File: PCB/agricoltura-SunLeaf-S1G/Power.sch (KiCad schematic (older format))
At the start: 0 parts

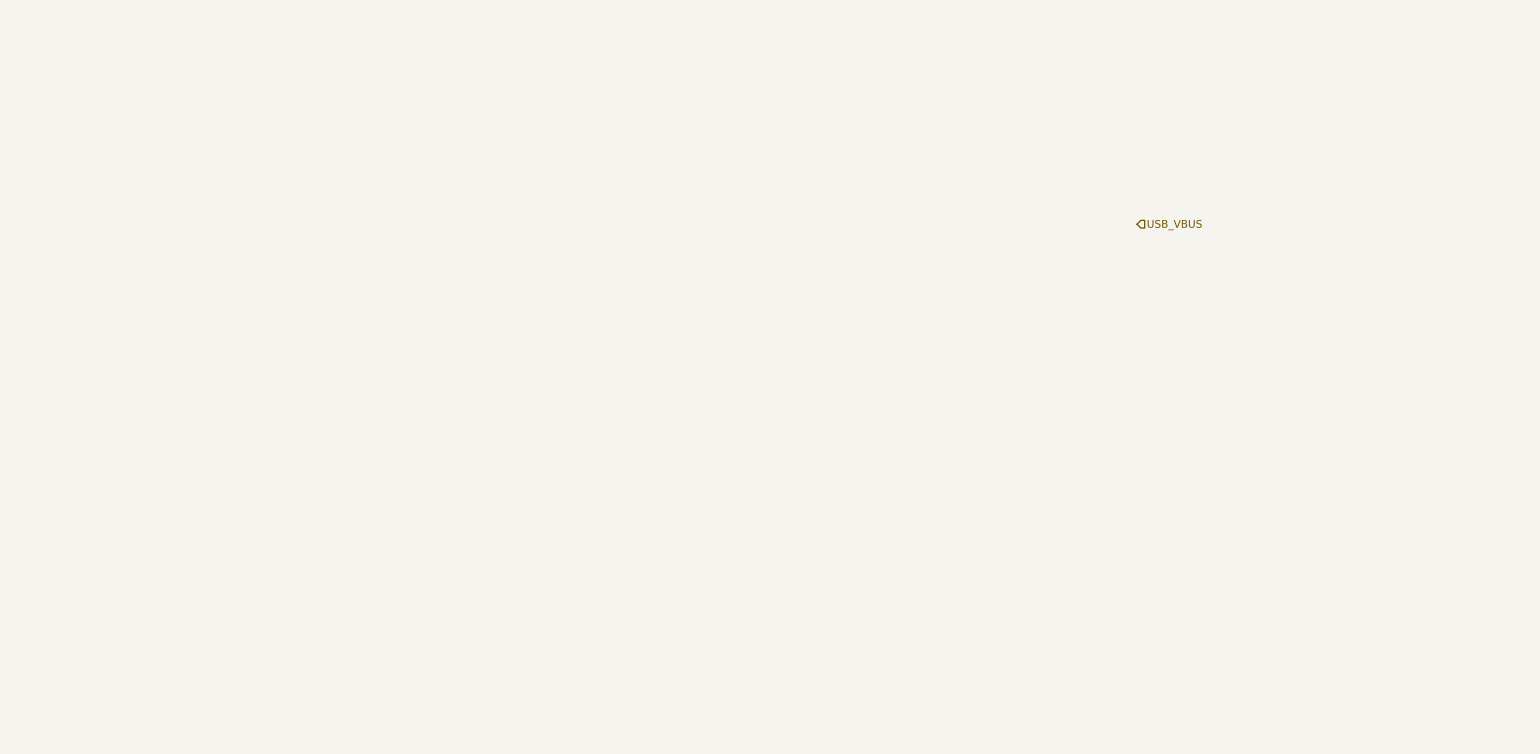
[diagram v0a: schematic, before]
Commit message: Power Supply and Datasheets
Added datasheets for parts in use, designed power supply circuit
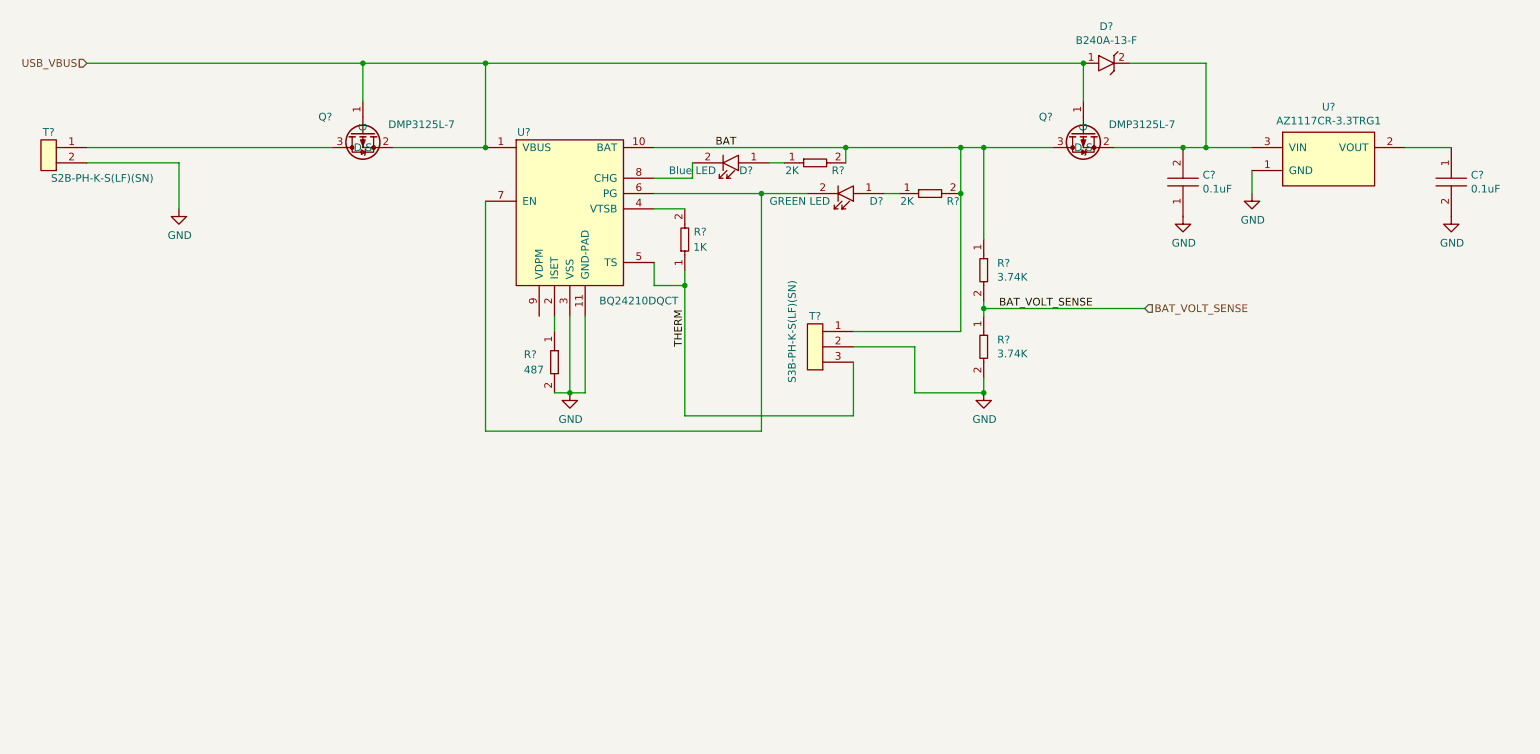
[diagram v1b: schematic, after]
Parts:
- added C?: C0402C104K9PACTU, AVR-KiCAD-Lib-Resistors:R0402, symbol AVR-KiCAD-Lib-Capacitors:C0402C104K9PACTU
- added C?: C0805C104M5RACTU, AVR-KiCAD-Lib-Capacitors:C0805, symbol AVR-KiCAD-Lib-Capacitors:C0805C104M5RACTU
- added D?: LTST-C194TBKT, AVR-KiCAD-Lib-Diodes:LED0603, symbol AVR-KiCAD-Lib-Diodes:LTST-C194TBKT
- added D?: LTST-C194KGKT, AVR-KiCAD-Lib-Diodes:LED0603, symbol AVR-KiCAD-Lib-Diodes:LTST-C194KGKT
- added D?: B240A-13-F, AVR-KiCAD-Lib-Diodes:B240A-13-F, symbol AVR-KiCAD-Lib-Diodes:B240A-13-F
- added Q? (x2): DMP3125L-7, growbox-KiCAD-Transistors:SOT-23, symbol AVR-KiCAD-Lib-Transistors:DMP3125L-7
- added R? (x2): RC0402FR-072KL, AVR-KiCAD-Lib-Resistors:R0402, symbol AVR-KiCAD-Lib-Resistors:RC0402FR-072KL
- added R?: RC0402FR-071KL, AVR-KiCAD-Lib-Resistors:R0402, symbol AVR-KiCAD-Lib-Resistors:RC0402FR-071KL
- added R? (x2): ERA-3AEB3741V, AVR-KiCAD-Lib-Resistors:R0603, symbol AVR-KiCAD-Lib-Resistors:ERA-3AEB3741V
- added R?: RC0402FR-07487RL, AVR-KiCAD-Lib-Resistors:R0402, symbol AVR-KiCAD-Lib-Resistors:RC0402FR-07487RL
- added T?: S2B-PH-K-S(LF)(SN), AVR-KiCAD-Lib-Connectors:S2B-PH-K-S(LF)(SN), symbol AVR-KiCAD-Lib-Connectors:S2B-PH-K-S(LF)(SN)
- added T?: S3B-PH-K-S(LF)(SN), AVR-KiCAD-Lib-Connectors:S3B-PH-K-S(LF)(SN), symbol AVR-KiCAD-Lib-Connectors:S3B-PH-K-S(LF)(SN)
- added U?: BQ24210DQCT, growbox-KiCAD-ICs:BQ24210, symbol AVR-KiCAD-Lib-ICs:BQ24210DQCT
- added U?: AZ1117CR-3.3TRG1, AVR-KiCAD-Lib-ICs:SOT_89, symbol AVR-KiCAD-Lib-ICs:AZ1117CR-3.3TRG1
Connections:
- net USB_VBUS: now also D?.1, Q?.1 (G), Q?.1 (G), Q?.2 (S), U?.1 (VBUS)
- new net: Q?.3 (D), T?.1
- new net: R?.1, U?.2 (ISET)
- new net: R?.2, U?.4 (VTSB)
- new net: D?.2, U?.6 (PG), U?.7 (EN)
- new net: D?.2, U?.8 (CHG)
- new net: D?.1, R?.1 (x2)
- new net: C?.1, U?.2 (VOUT)
- new net: C?.2, D?.2, Q?.2 (S), U?.3 (VIN)
- new net BAT: Q?.3 (D), R?.1, R?.2, R?.2, T?.1, U?.10 (BAT)
- new net BAT_VOLT_SENSE: R?.1, R?.2
- new net GND: C?.1, C?.2, R?.2, R?.2, T?.2, T?.2, U?.1 (GND), U?.11 (GND-PAD), U?.3 (VSS)
- new net THERM: R?.1, T?.3, U?.5 (TS)

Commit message: Schematic Complete
Schematic completed and PCB started
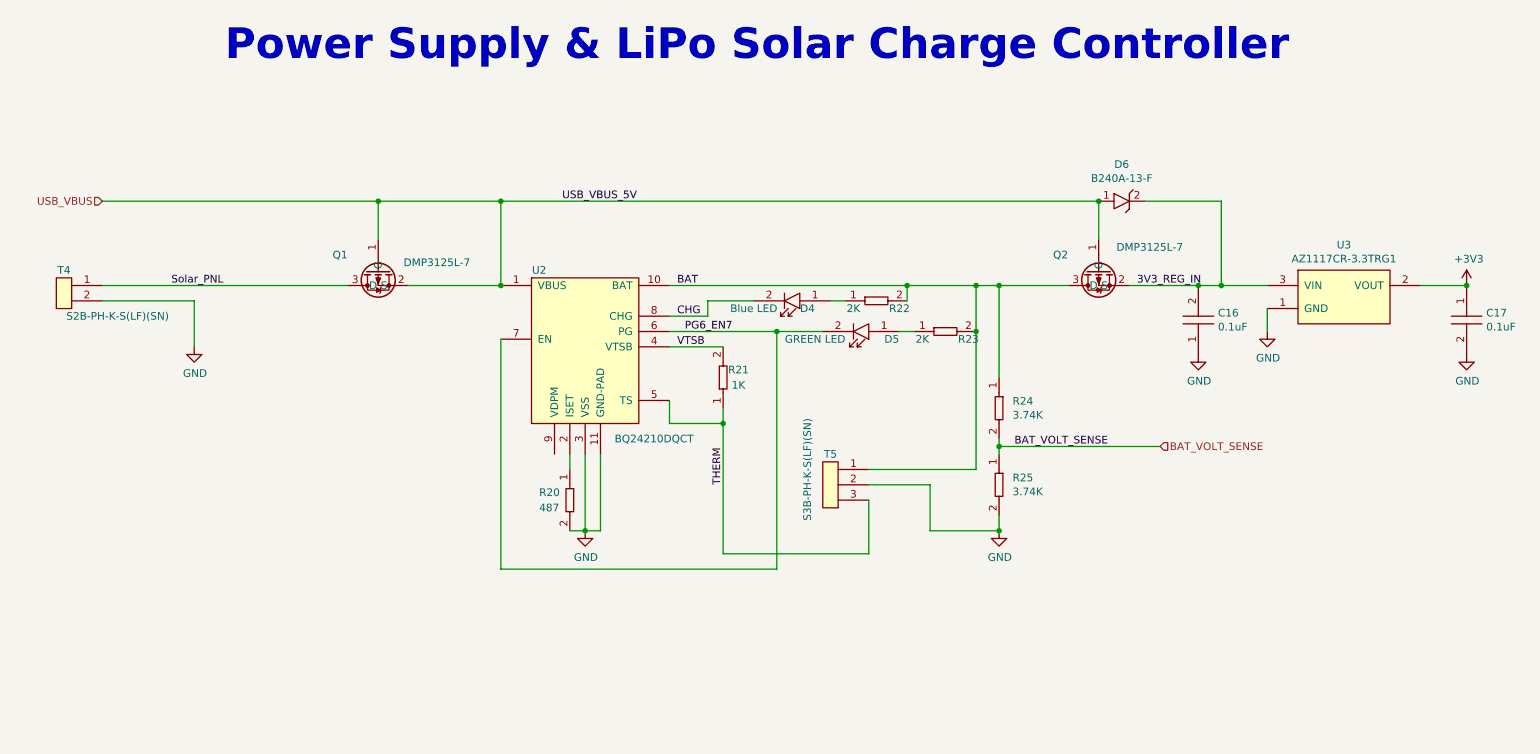
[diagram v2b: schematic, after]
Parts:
- gave numbers to parts that had none: 17
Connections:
- net Solar_PNL: now reaches Q1.3 (D), T4.1
- net VTSB: now reaches R21.2, U2.4 (VTSB)
- net PG6_EN7: now reaches D5.2, U2.6 (PG), U2.7 (EN)
- net CHG: now reaches D4.2, U2.8 (CHG)
- net +3V3: now reaches C17.1, U3.2 (VOUT)
- net 3V3_REG_IN: now reaches C16.2, D6.2, Q2.2 (S), U3.3 (VIN)
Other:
- note added: "Power Supply & LiPo Solar Charge Controller"
- moved on the sheet: C16, C17, D4, D5, D6, Q1, Q2, R20, R21, R22, R23, R24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

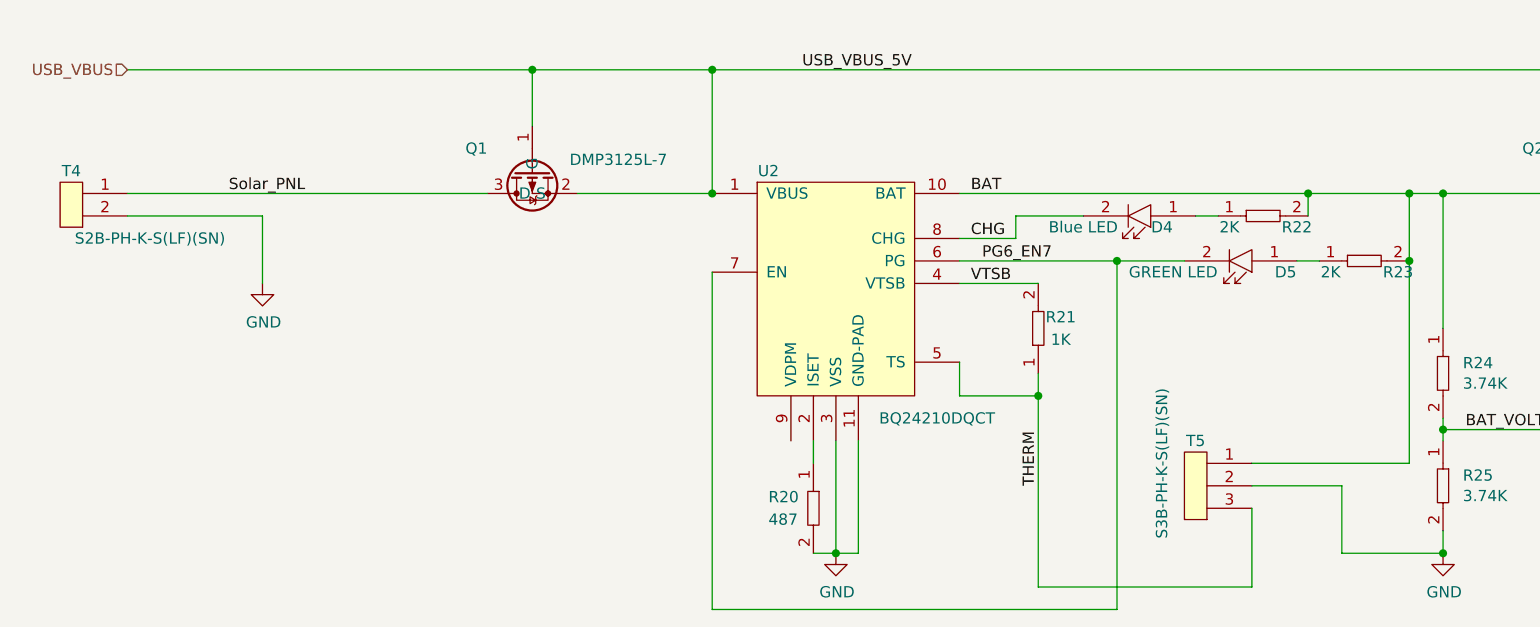
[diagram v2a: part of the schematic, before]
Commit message: PCB Progress
added TVS diodes fo QWIIC connector serial signals. Did more routing overall.
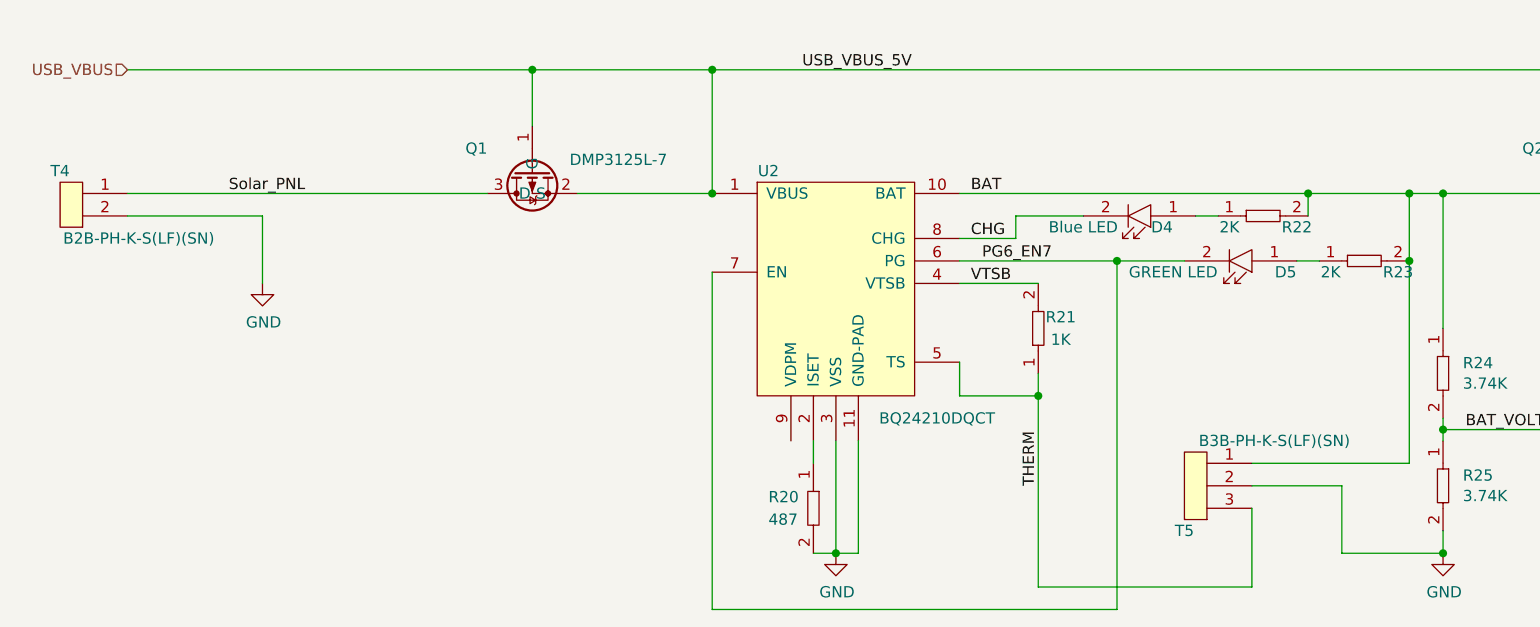
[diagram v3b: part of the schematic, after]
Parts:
- removed T4: S2B-PH-K-S(LF)(SN), AVR-KiCAD-Lib-Connectors:S2B-PH-K-S(LF)(SN), symbol AVR-KiCAD-Lib-Connectors:S2B-PH-K-S(LF)(SN)
- removed T5: S3B-PH-K-S(LF)(SN), AVR-KiCAD-Lib-Connectors:S3B-PH-K-S(LF)(SN), symbol AVR-KiCAD-Lib-Connectors:S3B-PH-K-S(LF)(SN)
- added T4: B2B-PH-K-S(LF)(SN), AVR-KiCAD-Lib-Connectors:B2B-PH-K-S(LF)(SN), symbol AVR-KiCAD-Lib-Connectors:B2B-PH-K-S(LF)(SN)
- added T5: B3B-PH-K-S(LF)(SN), AVR-KiCAD-Lib-Connectors:B3B-PH-K-S(LF)(SN), symbol AVR-KiCAD-Lib-Connectors:B3B-PH-K-S(LF)(SN)
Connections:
- net BAT: now also T5.1
- net GND: now also T4.2, T5.2
- net Solar_PNL: now also T4.1
- net THERM: now also T5.3
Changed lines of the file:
@@
-$EndComp
-$Comp
-L AVR-KiCAD-Lib-Connectors:S3B-PH-K-S(LF)(SN) T5
-U 1 1 5F07EF2F
-P 6400 4900
-F 0 "T5" H 6450 4950 50  0000 C CNN
-F 1 "S3B-PH-K-S(LF)(SN)" V 6300 4850 50  0000 C CNN
-F 2 "AVR-KiCAD-Lib-Connectors:S3B-PH-K-S(LF)(SN)" H 5100 5950 50  0001 C CNN
-F 3 "http://www.jst-mfg.com/product/pdf/eng/ePH.pdf" H 6300 5000 50  0001 C CNN
-F 4 "0.18000" H 6500 5150 50  0001 C CNN "Cost QTY: 1"
-F 5 "0.08119" H 6600 5250 50  0001 C CNN "Cost QTY: 1000"
-F 6 "*" H 6700 5350 50  0001 C CNN "Cost QTY: 2500"
-F 7 "0.07217" H 6800 5450 50  0001 C CNN "Cost QTY: 5000"
-F 8 "0.06541" H 6900 5550 50  0001 C CNN "Cost QTY: 10000"
-F 9 "JST Sales America Inc." H 7000 5650 50  0001 C CNN "MFR"
-F 10 "S3B-PH-K-S(LF)(SN)" H 7100 5750 50  0001 C CNN "MFR#"
-F 11 "Digikey" H 7200 5850 50  0001 C CNN "Vendor"
-F 12 "455-1720-ND" H 7300 5950 50  0001 C CNN "Vendor #"
-F 13 "AVR" H 7400 6050 50  0001 C CNN "Designer"
-F 14 "6mm" H 7500 6150 50  0001 C CNN "Height"
-F 15 "7/9/2020" H 8600 7250 50  0001 C CNN "Date Created"
-F 16 "7/9/2020" H 7600 6250 50  0001 C CNN "Date Modified"
-F 17 "Yes" H 7700 6350 50  0001 C CNN "Lead-Free ?"
-F 18 "1" H 7800 6450 50  0001 C CNN "RoHS Levels"
-F 19 "ThroughHole, RightAngle" H 7900 6550 50  0001 C CNN "Mounting"
-F 20 "3" H 8000 6650 50  0001 C CNN "Pin Count #"
-F 21 "Active" H 8100 6750 50  0001 C CNN "Status"
-F 22 "*" H 8200 6850 50  0001 C CNN "Tolerance"
-F 23 "Connector" H 8300 6950 50  0001 C CNN "Type"
-F 24 "100V" H 8400 7050 50  0001 C CNN "Voltage"
-F 25 "*" H 8500 7200 50  0001 C CNN "Package"
-F 26 "Connector Header Through Hole, Right Angle 3 position 0.079\" (2.00mm)" H 8900 7600 50  0001 C CNN "Description"
-F 27 "S3B-PH-K-S(LF)(SN)" H 8700 7400 50  0001 C CNN "_Value_"
-F 28 "*" H 8800 7500 50  0001 C CNN "Management_ID"
-	1    6400 4900
-	1    0    0    -1
-$EndComp
-$Comp
-L AVR-KiCAD-Lib-Connectors:S2B-PH-K-S(LF)(SN) T4
-U 1 1 5F07DDDE
-P 1400 3700
-F 0 "T4" H 1450 3750 50  0000 C CNN
-F 1 "S2B-PH-K-S(LF)(SN)" H 1800 3450 50  0000 C CNN
-F 2 "AVR-KiCAD-Lib-Connectors:S2B-PH-K-S(LF)(SN)" H 100 4750 50  0001 C CNN
-F 3 "http://www.jst-mfg.com/product/pdf/eng/ePH.pdf" H 1300 3800 50  0001 C CNN
-F 4 "0.17000" H 1500 3950 50  0001 C CNN "Cost QTY: 1"
-F 5 "0.07177" H 1600 4050 50  0001 C CNN "Cost QTY: 1000"
-F 6 "*" H 1700 4150 50  0001 C CNN "Cost QTY: 2500"
-F 7 "0.06152" H 1800 4250 50  0001 C CNN "Cost QTY: 5000"
-F 8 "0.05981" H 1900 4350 50  0001 C CNN "Cost QTY: 10000"
-F 9 "JST Sales America Inc." H 2000 4450 50  0001 C CNN "MFR"
-F 10 "S2B-PH-K-S(LF)(SN)" H 2100 4550 50  0001 C CNN "MFR#"
-F 11 "Digikey" H 2200 4650 50  0001 C CNN "Vendor"
-F 12 "455-1720-ND" H 2300 4750 50  0001 C CNN "Vendor #"
-F 13 "AVR" H 2400 4850 50  0001 C CNN "Designer"
-F 14 "6mm" H 2500 4950 50  0001 C CNN "Height"
-F 15 "7/9/2020" H 3600 6050 50  0001 C CNN "Date Created"
-F 16 "7/9/2020" H 2600 5050 50  0001 C CNN "Date Modified"
-F 17 "Yes" H 2700 5150 50  0001 C CNN "Lead-Free ?"
-F 18 "1" H 2800 5250 50  0001 C CNN "RoHS Levels"
-F 19 "ThroughHole, RightAngle" H 2900 5350 50  0001 C CNN "Mounting"
-F 20 "2" H 3000 5450 50  0001 C CNN "Pin Count #"
-F 21 "Active" H 3100 5550 50  0001 C CNN "Status"
-F 22 "*" H 3200 5650 50  0001 C CNN "Tolerance"
-F 23 "Connector" H 3300 5750 50  0001 C CNN "Type"
-F 24 "100V" H 3400 5850 50  0001 C CNN "Voltage"
-F 25 "*" H 3500 6000 50  0001 C CNN "Package"
-F 26 "Connector Header Through Hole, Right Angle 2 position 0.079\" (2.00mm)" H 3900 6400 50  0001 C CNN "Description"
-F 27 "S2B-PH-K-S(LF)(SN)" H 3700 6200 50  0001 C CNN "_Value_"
-F 28 "*" H 3800 6300 50  0001 C CNN "Management_ID"
-	1    1400 3700
-	1    0    0    -1
 $EndComp
 $Comp
@@
 Text Notes 2500 2300 0    200  ~ 40
 Power Supply & LiPo Solar Charge Controller
+$Comp
+L AVR-KiCAD-Lib-Connectors:B2B-PH-K-S(LF)(SN) T4
+U 1 1 5F6292FD
+P 1400 3700
+F 0 "T4" H 1400 3750 50  0000 C CNN
+F 1 "B2B-PH-K-S(LF)(SN)" H 1750 3450 50  0000 C CNN
+F 2 "AVR-KiCAD-Lib-Connectors:B2B-PH-K-S(LF)(SN)" H 100 4750 50  0001 C CNN
+F 3 "http://www.jst-mfg.com/product/pdf/eng/ePH.pdf" H 1300 3800 50  0001 C CNN
+F 4 "0.17000" H 1500 3950 50  0001 C CNN "Cost QTY: 1"
+F 5 "0.07252" H 1600 4050 50  0001 C CNN "Cost QTY: 1000"
+F 6 "*" H 1700 4150 50  0001 C CNN "Cost QTY: 2500"
+F 7 "0.06216" H 1800 4250 50  0001 C CNN "Cost QTY: 5000"
+F 8 "0.06044" H 1900 4350 50  0001 C CNN "Cost QTY: 10000"
+F 9 "JST Sales America Inc." H 2000 4450 50  0001 C CNN "MFR"
+F 10 "B2B-PH-K-S(LF)(SN)" H 2100 4550 50  0001 C CNN "MFR#"
+F 11 "Digikey" H 2200 4650 50  0001 C CNN "Vendor"
+F 12 "455-1704-ND" H 2300 4750 50  0001 C CNN "Vendor #"
+F 13 "AVR" H 2400 4850 50  0001 C CNN "Designer"
+F 14 "6mm" H 2500 4950 50  0001 C CNN "Height"
+F 15 "7/12/2020" H 3600 6050 50  0001 C CNN "Date Created"
+F 16 "7/12/2020" H 2600 5050 50  0001 C CNN "Date Modified"
+F 17 "Yes" H 2700 5150 50  0001 C CNN "Lead-Free ?"
+F 18 "1" H 2800 5250 50  0001 C CNN "RoHS Levels"
+F 19 "ThroughHole,Vertical" H 2900 5350 50  0001 C CNN "Mounting"
+F 20 "2" H 3000 5450 50  0001 C CNN "Pin Count #"
+F 21 "Active" H 3100 5550 50  0001 C CNN "Status"
+F 22 "*" H 3200 5650 50  0001 C CNN "Tolerance"
+F 23 "Connector" H 3300 5750 50  0001 C CNN "Type"
+F 24 "100V" H 3400 5850 50  0001 C CNN "Voltage"
+F 25 "*" H 3500 6000 50  0001 C CNN "Package"
+F 26 "Connector Header Through Hole 2 position 0.079\" (2.00mm)" H 3900 6400 50  0001 C CNN "Description"
+F 27 "B2B-PH-K-S(LF)(SN)" H 3700 6200 50  0001 C CNN "_Value_"
+F 28 "*" H 3800 6300 50  0001 C CNN "Management_ID"
+	1    1400 3700
+	1    0    0    -1
+$EndComp
+$Comp
+L AVR-KiCAD-Lib-Connectors:B3B-PH-K-S(LF)(SN) T5
+U 1 1 5F62B43B
+P 6400 4900
+F 0 "T5" H 6400 4550 50  0000 C CNN
+F 1 "B3B-PH-K-S(LF)(SN)" H 6800 4950 50  0000 C CNN
+F 2 "AVR-KiCAD-Lib-Connectors:B3B-PH-K-S(LF)(SN)" H 5100 5950 50  0001 C CNN
+F 3 "http://www.jst-mfg.com/product/pdf/eng/ePH.pdf" H 6300 5000 50  0001 C CNN
+F 4 "0.19000" H 6500 5150 50  0001 C CNN "Cost QTY: 1"
+F 5 "0.08736" H 6600 5250 50  0001 C CNN "Cost QTY: 1000"
+F 6 "*" H 6700 5350 50  0001 C CNN "Cost QTY: 2500"
+F 7 "0.07765" H 6800 5450 50  0001 C CNN "Cost QTY: 5000"
+F 8 "0.07037" H 6900 5550 50  0001 C CNN "Cost QTY: 10000"
+F 9 "JST Sales America Inc." H 7000 5650 50  0001 C CNN "MFR"
+F 10 "B3B-PH-K-S(LF)(SN)" H 7100 5750 50  0001 C CNN "MFR#"
+F 11 "Digikey" H 7200 5850 50  0001 C CNN "Vendor"
+F 12 "455-1705-ND" H 7300 5950 50  0001 C CNN "Vendor #"
+F 13 "AVR" H 7400 6050 50  0001 C CNN "Designer"
+F 14 "6mm" H 7500 6150 50  0001 C CNN "Height"
+F 15 "7/12/2020" H 8600 7250 50  0001 C CNN "Date Created"
+F 16 "7/12/2020" H 7600 6250 50  0001 C CNN "Date Modified"
+F 17 "Yes" H 7700 6350 50  0001 C CNN "Lead-Free ?"
+F 18 "1" H 7800 6450 50  0001 C CNN "RoHS Levels"
+F 19 "ThroughHole, Vertical" H 7900 6550 50  0001 C CNN "Mounting"
+F 20 "3" H 8000 6650 50  0001 C CNN "Pin Count #"
+F 21 "Active" H 8100 6750 50  0001 C CNN "Status"
+F 22 "*" H 8200 6850 50  0001 C CNN "Tolerance"
+F 23 "Connector" H 8300 6950 50  0001 C CNN "Type"
+F 24 "100V" H 8400 7050 50  0001 C CNN "Voltage"
+F 25 "*" H 8500 7200 50  0001 C CNN "Package"
+F 26 "Connector Header Through Hole 3 position 0.079\" (2.00mm)" H 8900 7600 50  0001 C CNN "Description"
+F 27 "B3B-PH-K-S(LF)(SN)" H 8700 7400 50  0001 C CNN "_Value_"
+F 28 "*" H 8800 7500 50  0001 C CNN "Management_ID"
+	1    6400 4900
+	1    0    0    -1
+$EndComp
 $EndSCHEMATC
